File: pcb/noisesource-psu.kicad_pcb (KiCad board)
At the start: 2 copper layers, 40 x 25 mm, 22 parts, among them J1 USB_B_Micro, J2 Conn_Coaxial, U1 FT230XS, U2 TPS22917DBV, U4 TLV61046ADB

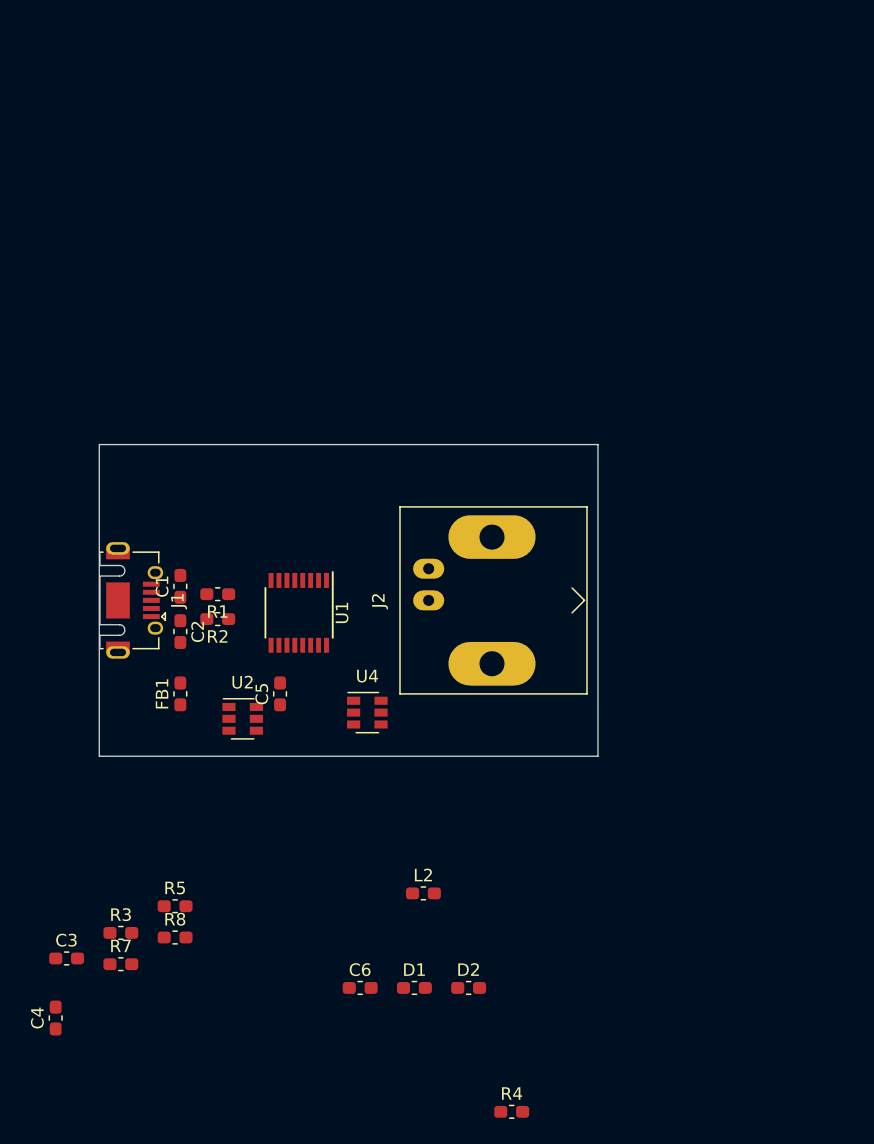
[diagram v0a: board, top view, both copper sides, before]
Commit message: schematic: Added output filter, added footprints
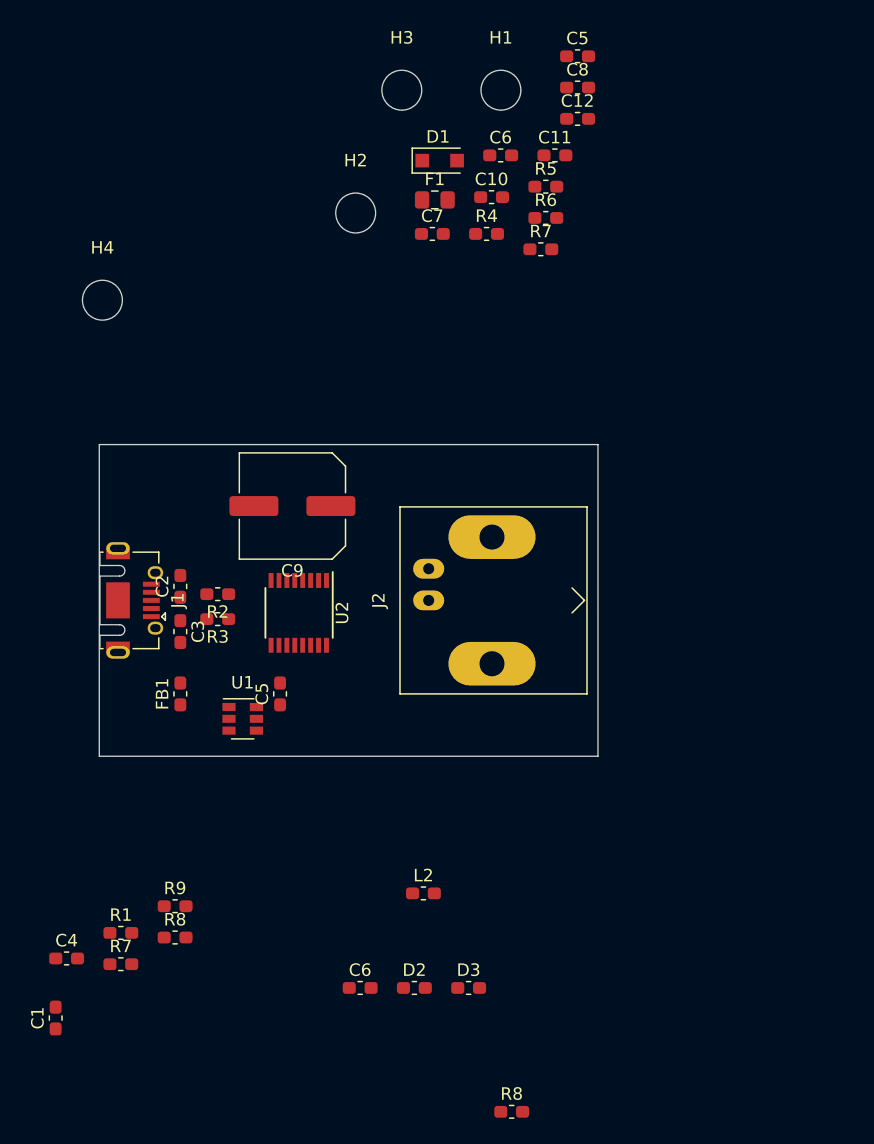
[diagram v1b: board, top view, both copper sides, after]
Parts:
- removed U4: TLV61046ADB, Package_TO_SOT_SMD:SOT-23-6
- added C10: 1uF, Capacitor_SMD:C_0603_1608Metric_Pad1.05x0.95mm_HandSolder, F.Cu at (126.5, 50.2)
- added C11: 10uF, Capacitor_SMD:C_0603_1608Metric_Pad1.05x0.95mm_HandSolder, F.Cu at (131.5, 46.8)
- added C12: 10uF, Capacitor_SMD:C_0603_1608Metric_Pad1.05x0.95mm_HandSolder, F.Cu at (133.4, 43.9)
- added C5: 10uF, Capacitor_SMD:C_0603_1608Metric_Pad1.05x0.95mm_HandSolder, F.Cu at (133.4, 38.9)
- added C6: 10uF, Capacitor_SMD:C_0603_1608Metric_Pad1.05x0.95mm_HandSolder, F.Cu at (127.2, 46.8)
- added C7: 100nF, Capacitor_SMD:C_0603_1608Metric_Pad1.05x0.95mm_HandSolder, F.Cu at (121.7, 53.1)
- added C8: 680pF, Capacitor_SMD:C_0603_1608Metric_Pad1.05x0.95mm_HandSolder, F.Cu at (133.4, 41.4)
- added C9: 47uF, Capacitor_SMD:C_Elec_8x6.2, F.Cu at (110.5, 74.9)
- added D1: SS14FL, Diode_SMD:D_SOD-123F, F.Cu at (122.3, 47.2)
- added F1: Polyfuse, Fuse:Fuse_0805_2012Metric_Pad1.15x1.40mm_HandSolder, F.Cu at (121.9, 50.4)
- added H1: MountingHole, MountingHole:MountingHole_3.2mm_M3, F.Cu at (127.2, 41.6)
- added H2: MountingHole, MountingHole:MountingHole_3.2mm_M3, F.Cu at (115.6, 51.4)
- added H3: MountingHole, MountingHole:MountingHole_3.2mm_M3, F.Cu at (119.3, 41.6)
- added H4: MountingHole, MountingHole:MountingHole_3.2mm_M3, F.Cu at (95.2, 58.4)
- added R4: 86.6k, Resistor_SMD:R_0603_1608Metric_Pad1.05x0.95mm_HandSolder, F.Cu at (126.1, 53.1)
- added R5: 28.7k, Resistor_SMD:R_0603_1608Metric_Pad1.05x0.95mm_HandSolder, F.Cu at (130.8, 49.3)
- added R6: 357k, Resistor_SMD:R_0603_1608Metric_Pad1.05x0.95mm_HandSolder, F.Cu at (130.8, 51.8)
- added R7: 16.2k, Resistor_SMD:R_0603_1608Metric_Pad1.05x0.95mm_HandSolder, F.Cu at (130.4, 54.3)
- C1: renamed from C4; footprint Resistor_SMD:R_0603_1608Metric_Pad1.05x0.95mm_HandSolder -> Capacitor_SMD:C_0603_1608Metric_Pad1.05x0.95mm_HandSolder
- C2: renamed from C1; footprint Resistor_SMD:R_0603_1608Metric_Pad1.05x0.95mm_HandSolder -> Capacitor_SMD:C_0603_1608Metric_Pad1.05x0.95mm_HandSolder
- C3: renamed from C2; footprint Resistor_SMD:R_0603_1608Metric_Pad1.05x0.95mm_HandSolder -> Capacitor_SMD:C_0603_1608Metric_Pad1.05x0.95mm_HandSolder
- C4: renamed from C3; footprint Resistor_SMD:R_0603_1608Metric_Pad1.05x0.95mm_HandSolder -> Capacitor_SMD:C_0603_1608Metric_Pad1.05x0.95mm_HandSolder
- renumbered D1 to D2, D2 to D3, R3 to R1, R1 to R2, R2 to R3, R4 to R8, R5 to R9, U2 to U1, U1 to U2
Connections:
- FB1 pad 2: Net-(FB1-Pad2) -> Net-(F1-Pad2)
- J1 pad 1: Net-(FB1-Pad2) -> Net-(F1-Pad1)
- J2 pad 1: Net-(C6-Pad1) -> Net-(C12-Pad1)
- R1 pad 2: Net-(C5-Pad1) -> Net-(C5-Pad2)
- U1 pad 6: Net-(C5-Pad1) -> Net-(C5-Pad2)

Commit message: pcb: Updated schematic and layout
Schematic:
  Added testpoints
  Added ground pad to TPS51175

Layout:
  Completed initial layout of PCB
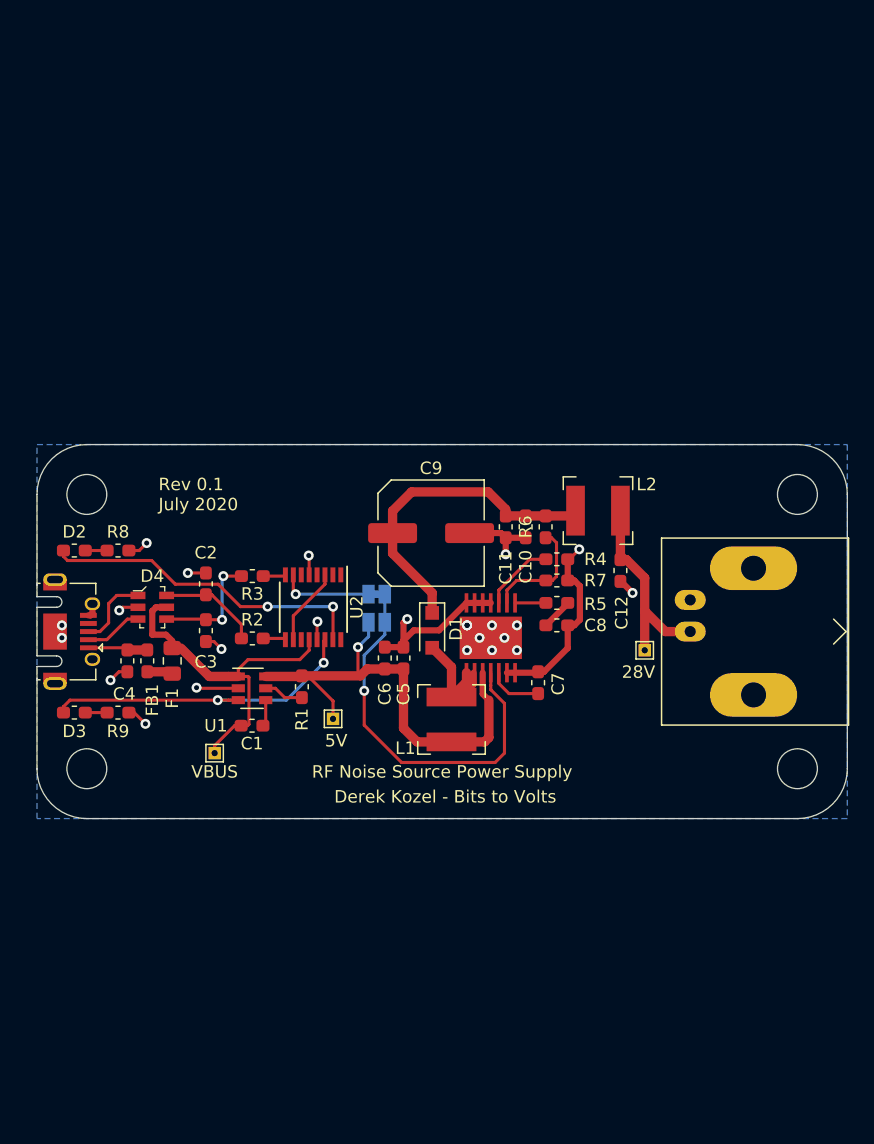
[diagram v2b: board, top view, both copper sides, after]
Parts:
- removed the C5 at (109.5, 90.0)
- removed the C6 at (115.9, 113.6)
- removed the R7 at (96.7, 111.7)
- removed the R8 at (101.1, 109.5)
- added 28V: TestPoint, TestPoint:TestPoint_THTPad_1.0x1.0mm_Drill0.5mm, F.Cu at (138.8, 86.5)
- added 5V: TestPoint, TestPoint:TestPoint_THTPad_1.0x1.0mm_Drill0.5mm, F.Cu at (113.8, 92.0)
- added D4: USBLC6-2SC6, digikey-footprints:SOT23-6L, F.Cu at (99.2, 83.0)
- added JP1: SolderJumper_2_Open, Jumper:SolderJumper-2_P1.3mm_Open_Pad1.0x1.5mm, B.Cu at (117.2, 84.2)
- added JP2: SolderJumper_2_Bridged, Jumper:SolderJumper-2_P1.3mm_Bridged_Pad1.0x1.5mm, B.Cu at (117.2, 82.0)
- added L1: 27uH, l_bourns-SRN5040:L_Bourns-SRN5040, F.Cu at (123.2, 92.0)
- added U3: TPS61175, tssop14:TSSOP14, F.Cu at (126.4, 85.5)
- added VBUS: TestPoint, TestPoint:TestPoint_THTPad_1.0x1.0mm_Drill0.5mm, F.Cu at (104.2, 94.8)
- C1: value C -> 100pF
- L2: value L -> 10uH; footprint Resistor_SMD:R_0603_1608Metric_Pad1.05x0.95mm_HandSolder -> l_bourns-SRN5040:L_Bourns-SRN5040
- R8, R9: value R -> 330
- moved H4 67.2 mm to (151.0, 96.0)
- moved H3 60.0 mm to (94.0, 96.0)
- moved R8 55.0 mm to (96.5, 78.5)
- moved C5 50.2 mm to (119.4, 87.1), turned to 270 degrees
- moved H1 46.4 mm to (94.0, 74.0)
- moved D2 44.4 mm to (93.0, 78.5), turned to 180 degrees
- moved C8 43.2 mm to (131.7, 84.5)
- moved F1 42.6 mm to (100.8, 87.3), turned to 90 degrees
- moved H2 42.0 mm to (151.0, 74.0)
- moved C6 41.4 mm to (117.9, 87.1), turned to 90 degrees
- moved D3 38.6 mm to (93.0, 91.5), turned to 180 degrees
- moved D1 37.7 mm to (121.7, 84.9), turned to 270 degrees
- moved C7 37.0 mm to (130.2, 89.1), turned to 90 degrees
- moved C12 36.4 mm to (136.8, 80.1), turned to 270 degrees
- moved L2 33.7 mm to (135.0, 75.3)
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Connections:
- C12 pad 1: Net-(C12-Pad1) -> Net-(28V1-Pad1)
- C4 pad 1: VBUS -> Net-(C4-Pad1)
- F1 pad 2: Net-(F1-Pad2) -> VBUS
- FB1 pad 1: VBUS -> Net-(F1-Pad1)
- FB1 pad 2: Net-(F1-Pad2) -> Net-(C4-Pad1)
- J1 pad 1: Net-(F1-Pad1) -> Net-(C4-Pad1)
- J1 pad 2: Net-(C3-Pad1) -> Net-(D4-Pad3)
- J1 pad 3: Net-(C2-Pad1) -> Net-(D4-Pad1)
- J2 pad 1: Net-(C12-Pad1) -> Net-(28V1-Pad1)
- L2 pad 1: Net-(C6-Pad1) -> Net-(C10-Pad1)
- L2 pad 2: Net-(L2-Pad2) -> Net-(28V1-Pad1)
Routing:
- net GND: track 0.00 -> 53.0 mm, vias 0 -> 24
- net Net-(5V1-Pad1): track 0.00 -> 38.4 mm, vias 0 -> 1
- net /TPS_EN: track 0.00 -> 30.9 mm, vias 0 -> 1
- net VBUS: track 0.00 -> 28.3 mm
- net /PWREN#: track 0.00 -> 26.4 mm, vias 0 -> 2
- net /Vout_EN: track 0.00 -> 26.4 mm, vias 0 -> 2
- net Net-(C10-Pad1): track 0.00 -> 26.1 mm
- net Net-(28V1-Pad1): track 0.00 -> 16.6 mm
- net Net-(D1-Pad2): track 0.00 -> 10.2 mm
- net Net-(C3-Pad1): track 0.00 -> 9.46 mm, vias 0 -> 2
- net Net-(R6-Pad1): track 0.00 -> 9.20 mm
- net Net-(C2-Pad1): track 0.00 -> 8.13 mm
- net Net-(JP2-Pad1): track 0.00 -> 7.48 mm, vias 0 -> 1
- net +3V3: track 0.00 -> 6.25 mm
- net Net-(D4-Pad1): track 0.00 -> 6.08 mm
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- added copper zone on B.Cu, net GND
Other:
- board size 40 x 25 mm -> 65 x 30 mm
- net class Default: trace_width 0.25 -> 0.5
- net class Power added: clearance 0.2, trace_width 1, via_dia 0.8, via_drill 0.4
- board text added: "Derek Kozel - Bits to Volts"
- board text added: "RF Noise Source Power Supply"
- board text added: "Rev 0.1 July 2020"

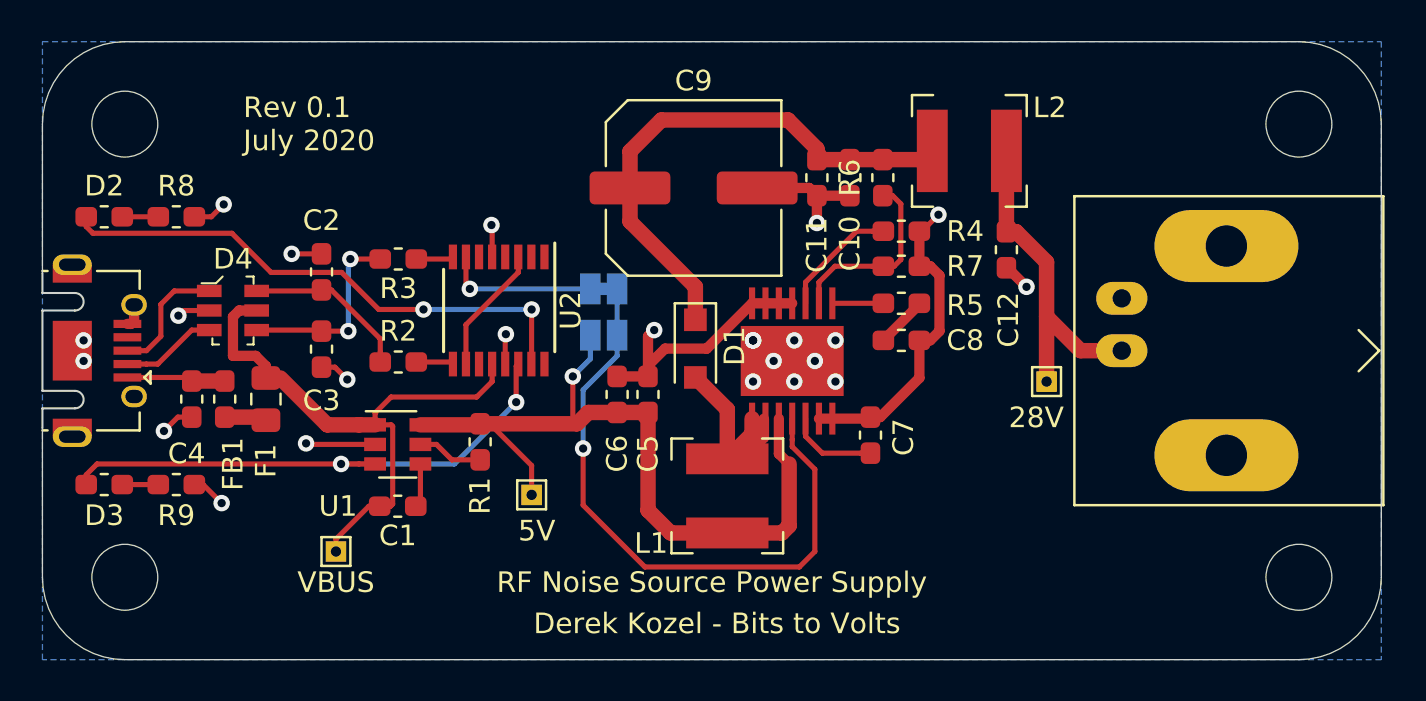
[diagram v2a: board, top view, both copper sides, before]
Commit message: pcb: Updated schematic and layout
Added 3.3v decoupling cap
Added top ground fill
Changed solder jumper footprint
Added sense and test load resistors
Changed SMPS ground pad to thermal fill
Changed mounting holes to plated through vias with pads
Moved test points
Misc rerouting
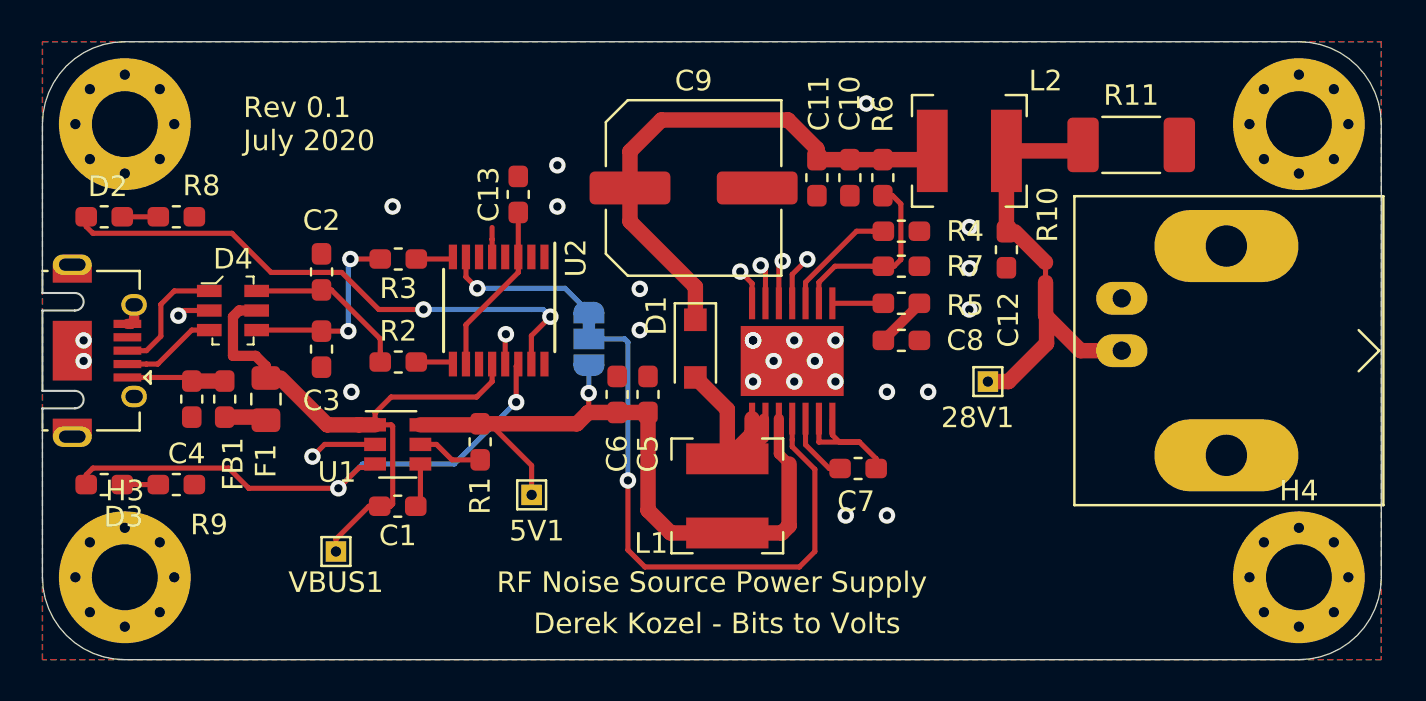
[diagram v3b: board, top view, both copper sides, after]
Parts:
- removed JP2: SolderJumper_2_Bridged, Jumper:SolderJumper-2_P1.3mm_Bridged_Pad1.0x1.5mm
- added C13: 10nF, Capacitor_SMD:C_0603_1608Metric_Pad1.05x0.95mm_HandSolder, F.Cu at (113.1, 77.4)
- added R10: 10, Resistor_SMD:R_0402_1005Metric, F.Cu at (138.7, 81.2)
- added R11: 460, Resistor_SMD:R_2010_5025Metric_Pad1.52x2.65mm_HandSolder, F.Cu at (142.9, 75.0)
- H1, H2, H3, H4: footprint MountingHole:MountingHole_3.2mm_M3 -> MountingHole:MountingHole_3.2mm_M3_Pad_Via
- JP1: value SolderJumper_2_Open -> SolderJumper_3_Bridged12; footprint Jumper:SolderJumper-2_P1.3mm_Open_Pad1.0x1.5mm -> Jumper:SolderJumper-3_P1.3mm_Bridged12_RoundedPad1.0x1.5mm
- R1: value R -> DNP
- moved 28V1 2.85 mm to (135.9, 86.5)
- moved C7 1.73 mm to (129.6, 90.7), turned to 0 degrees
- moved JP1 0.74 mm to (116.5, 84.4), turned to 270 degrees
- renumbered 28V to 28V1, 5V to 5V1, VBUS to VBUS1
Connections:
- H1 pad 1: (no net) -> GND
- H2 pad 1: (no net) -> GND
- H3 pad 1: (no net) -> GND
- H4 pad 1: (no net) -> GND
- JP1 pad 1: Net-(5V1-Pad1) -> /TPS_EN
- JP1 pad 2: /TPS_EN -> Net-(JP1-Pad2)
- U2 pad 7: Net-(JP2-Pad1) -> /TPS_EN
- U3 pad 4: /TPS_EN -> Net-(JP1-Pad2)
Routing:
- net Net-(JP1-Pad2): track 0.00 -> 28.7 mm, vias 0 -> 1
- net GND: track 53.0 -> 24.3 mm, vias 24 -> 32
- net /TPS_EN: track 30.9 -> 7.65 mm
- net Net-(JP2-Pad1): track 7.48 -> 0.00 mm, vias 1 -> 0
- net Net-(28V1-Pad1): track 16.6 -> 22.2 mm
- net Net-(5V1-Pad1): track 38.4 -> 36.0 mm
- net +3V3: track 6.25 -> 8.41 mm
- net /Vout_EN: track 26.4 -> 27.8 mm
- net /PWREN#: track 26.4 -> 27.5 mm
- net Net-(C7-Pad1): track 4.35 -> 3.42 mm
- added copper zone on F.Cu, net GND
